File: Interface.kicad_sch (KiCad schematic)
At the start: 39 parts, among them U11 WE-TVS-82400102, U2 SN74LVC2G14DBV, U6 THVD1400D, U7 TLP2310, U8 TLP2310

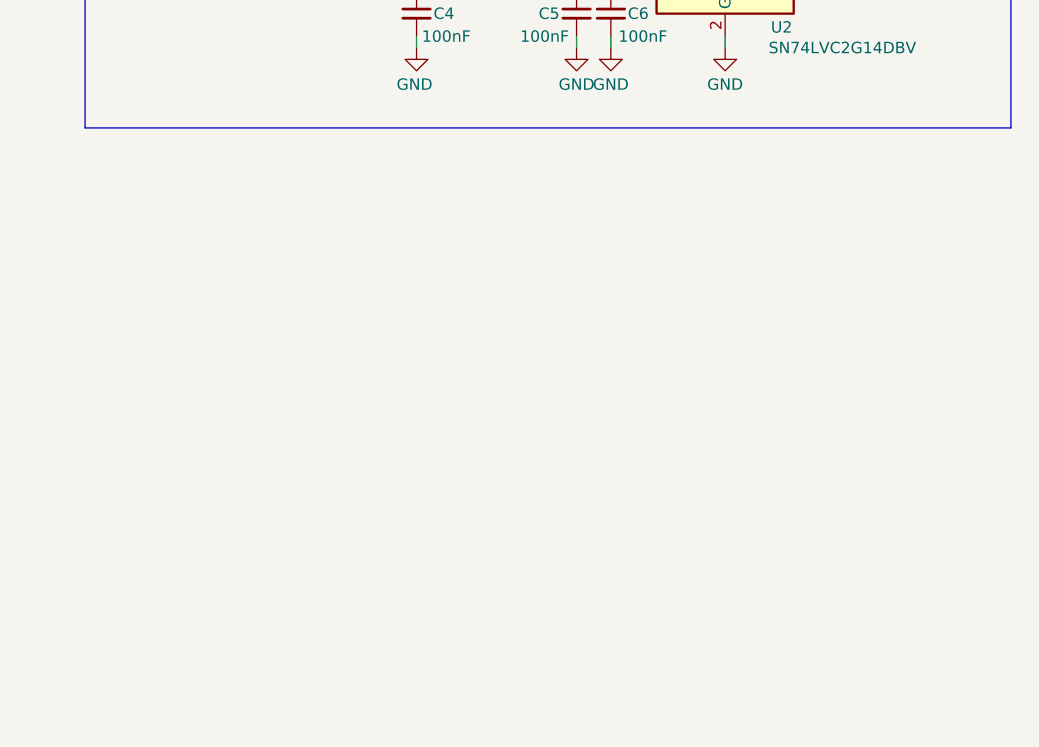
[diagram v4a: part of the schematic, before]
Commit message: feat(hw): add asymmetrical RC pulse stretcher for UART TX/RX activity LEDs
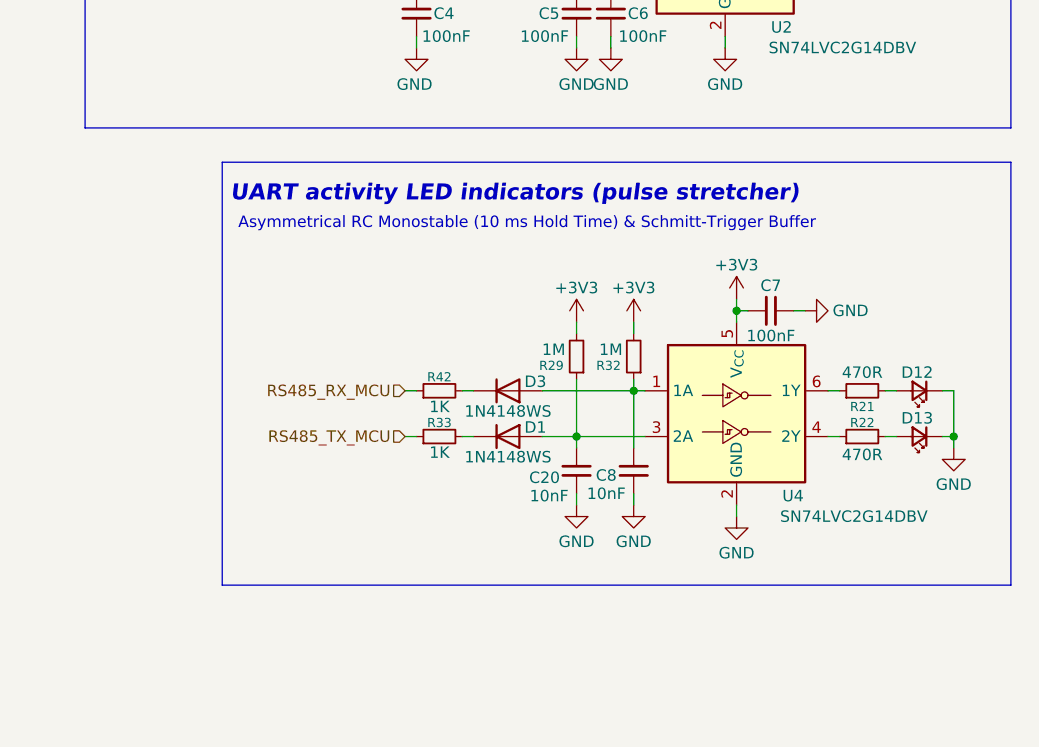
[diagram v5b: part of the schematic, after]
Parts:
- added C20, C8: 10nF, Capacitor_SMD:C_0603_1608Metric, symbol Device:C_Small
- added C7: 100nF, Capacitor_SMD:C_0603_1608Metric, symbol Device:C_Small
- added D1, D3: 1N4148WS, Diode_SMD:D_SOD-323, symbol Diode:1N4148WS
- added D12, D13: LED_Small, LED_SMD:LED_0603_1608Metric, symbol Device:LED_Small
- added R21, R22: 470R, Resistor_SMD:R_0603_1608Metric, symbol Device:R_Small
- added R29, R32: 1M, Resistor_SMD:R_0603_1608Metric, symbol Device:R_Small
- added R33, R42: 1K, Resistor_SMD:R_0603_1608Metric, symbol Device:R_Small
- added U4: SN74LVC2G14DBV, Package_TO_SOT_SMD:SOT-23-6, symbol 74xGxx:SN74LVC2G14DBV
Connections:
- net +3V3: now also C7.1, R29.2, R32.2, U4.5 (V_{CC})
- net GND: now also C20.1, C7.2, C8.1, D12.1 (K), D13.1 (K), U4.2 (GND)
- net RS485_RX_MCU: now also R42.1
- net RS485_TX_MCU: now also R33.1
- new net: C20.2, D1.2 (A), R29.1, U4.3 (2A)
- new net: R21.1, U4.6 (1Y)
- new net: D12.2 (A), R21.2
- new net: D1.1 (K), R33.2
- new net: C8.2, D3.2 (A), R32.1, U4.1 (1A)
- new net: R22.1, U4.4 (2Y)
- new net: D13.2 (A), R22.2
- new net: D3.1 (K), R42.2
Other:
- note added: "Asymmetrical RC Monostable (10 ms Hold Time) & Schmitt-Trigger Buffer"
- note added: "UART activity LED indicators (pulse stretcher)"

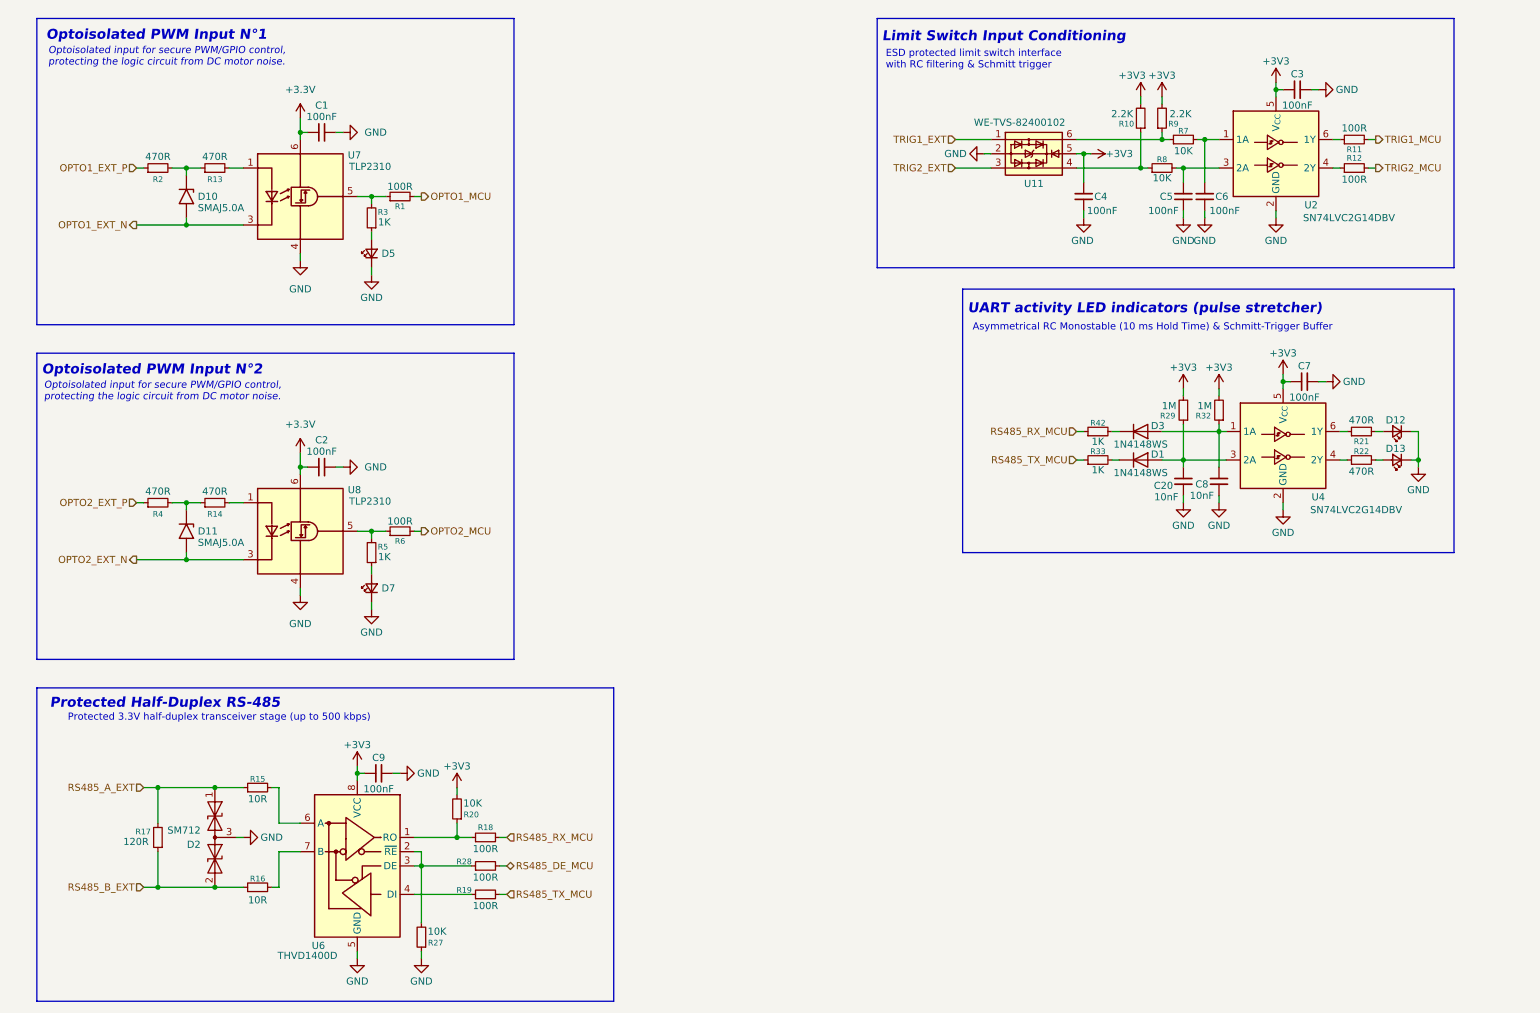
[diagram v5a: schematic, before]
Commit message: feat:add power sheat
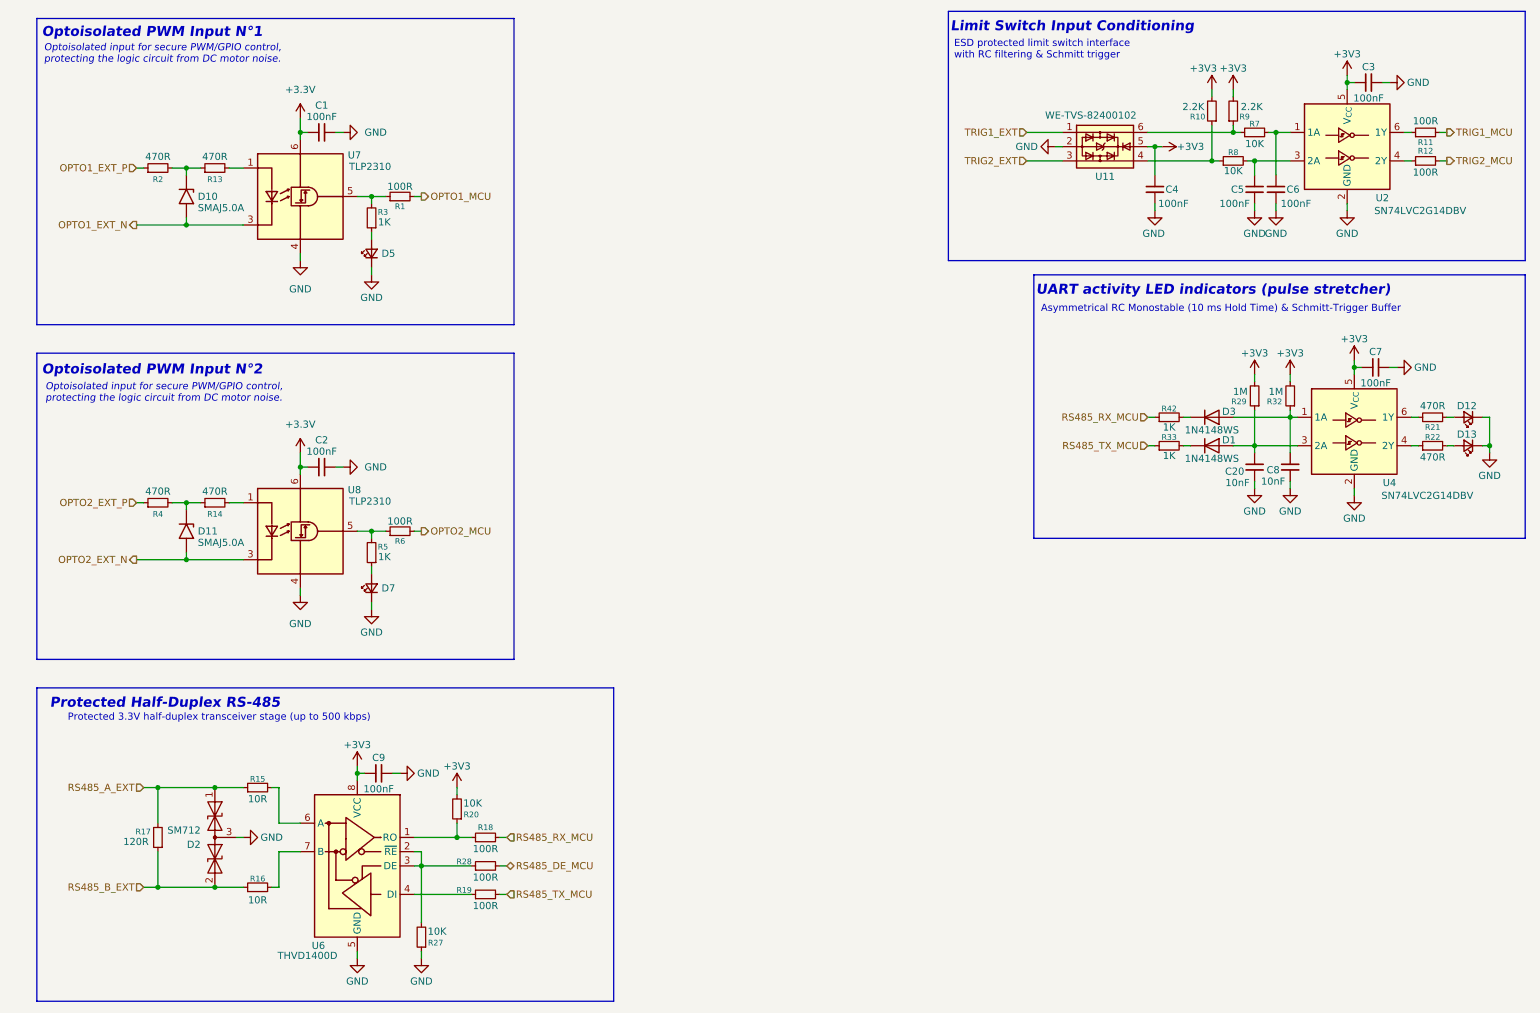
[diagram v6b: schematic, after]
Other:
- moved on the sheet: C20, C3, C4, C5, C6, C7, C8, D1, D12, D13, D3, R10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

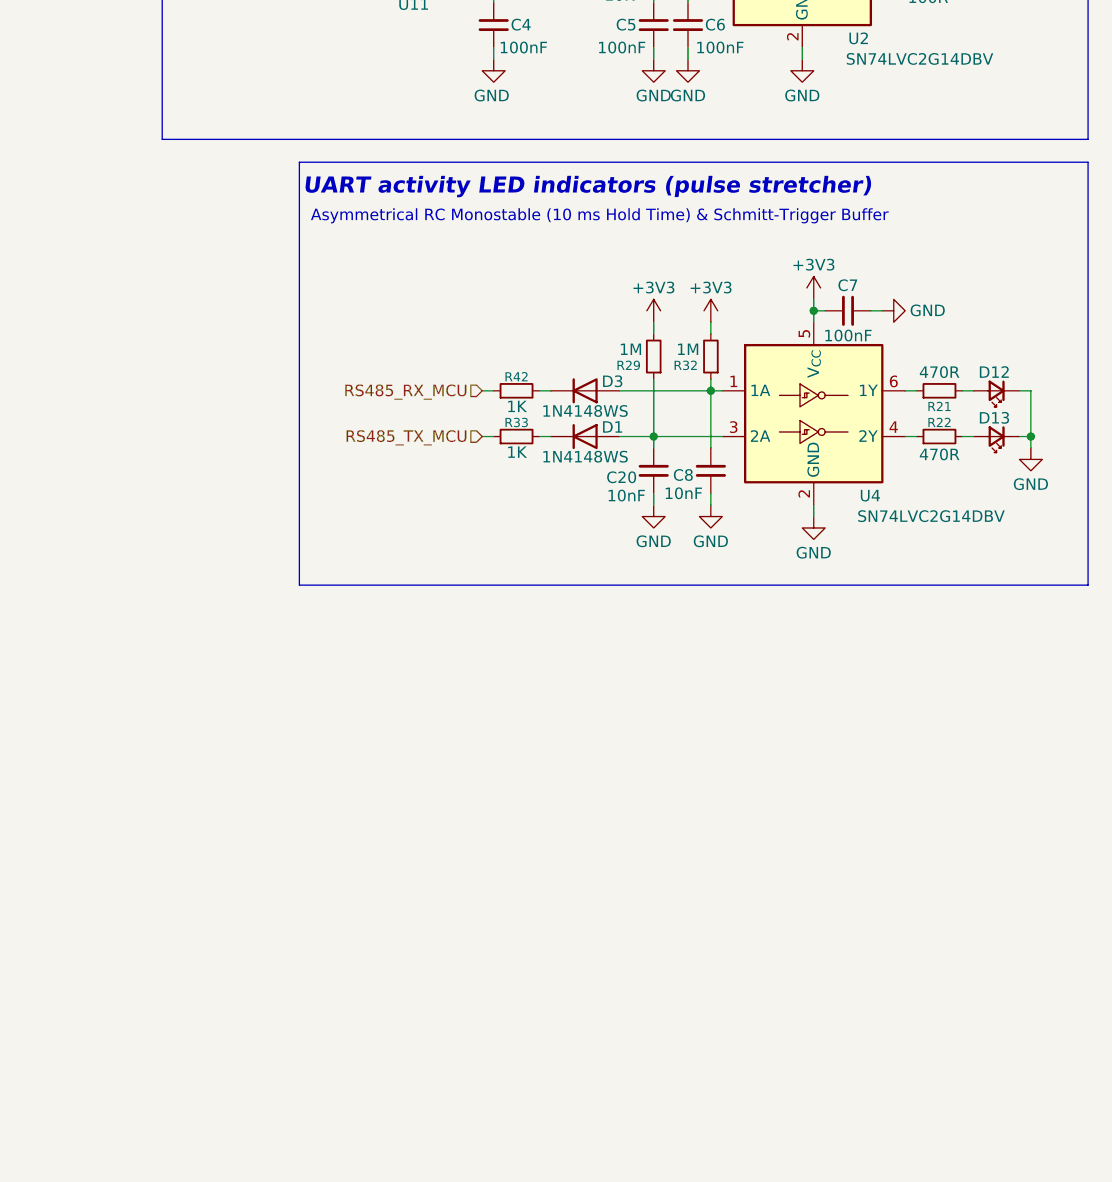
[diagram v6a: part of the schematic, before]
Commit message: feat: add quadrature encoder interface
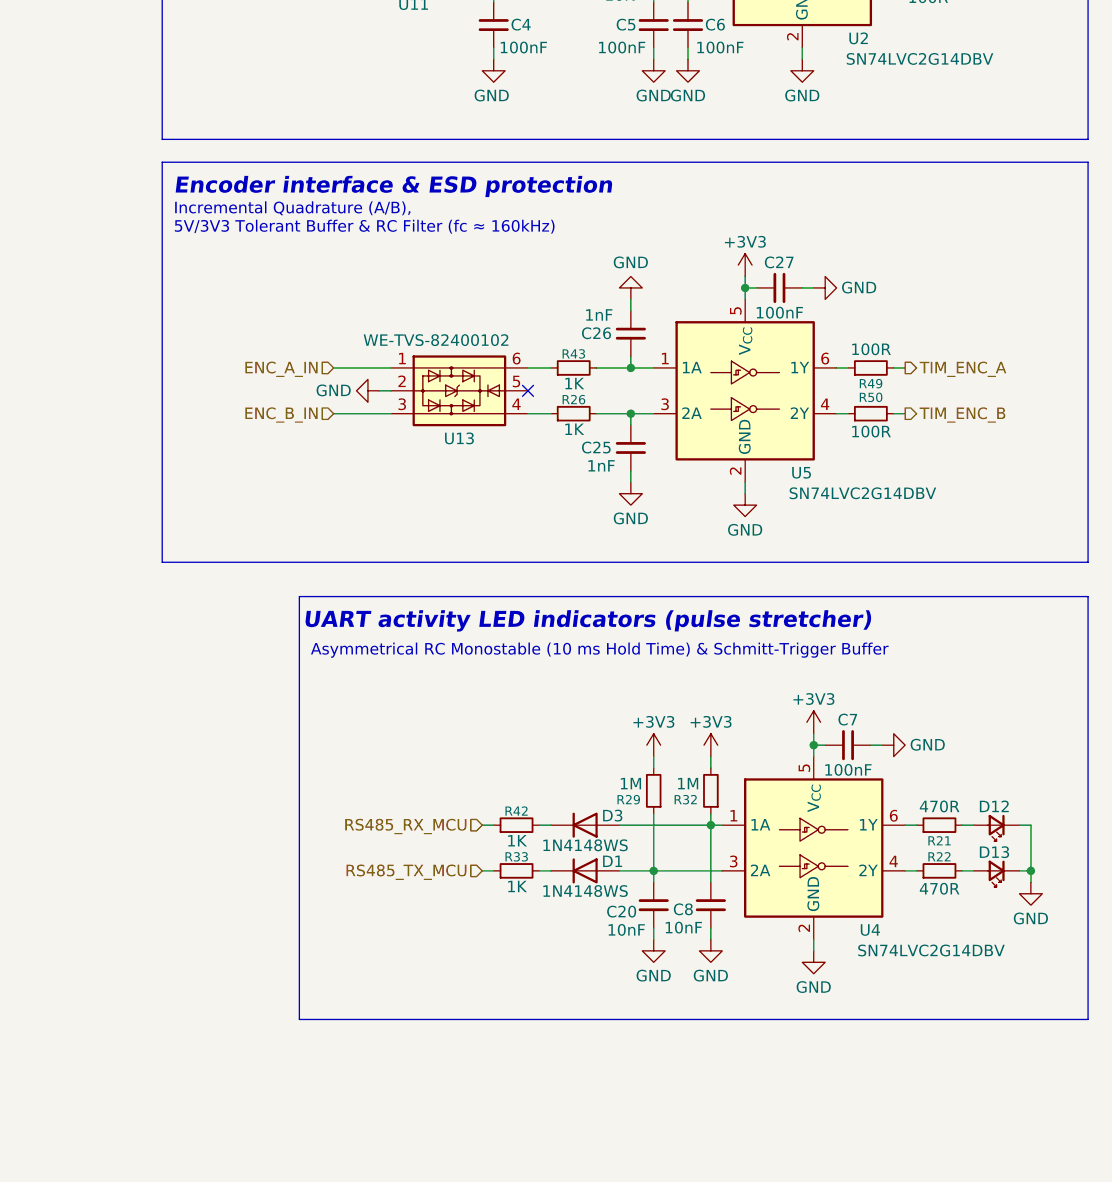
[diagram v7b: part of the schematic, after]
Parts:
- added C25, C26: 1nF, Capacitor_SMD:C_0603_1608Metric, symbol Device:C_Small
- added C27: 100nF, Capacitor_SMD:C_0603_1608Metric, symbol Device:C_Small
- added R26, R43: 1K, Resistor_SMD:R_0603_1608Metric, symbol Device:R_Small
- added R49, R50: 100R, Resistor_SMD:R_0603_1608Metric, symbol Device:R_Small
- added U13: WE-TVS-82400102, Package_TO_SOT_SMD:SOT-23-6, symbol Power_Protection:WE-TVS-82400102
- added U5: SN74LVC2G14DBV, Package_TO_SOT_SMD:SOT-23-6, symbol 74xGxx:SN74LVC2G14DBV
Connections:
- net +3V3: now also C27.1, U5.5 (V_{CC})
- net GND: now also C25.1, C26.1, C27.2, U13.2, U5.2 (GND)
- new net: R26.1, U13.4
- new net: C25.2, R26.2, U5.3 (2A)
- new net: R50.1, U5.4 (2Y)
- new net: C26.2, R43.2, U5.1 (1A)
- new net: R43.1, U13.6
- new net: R49.1, U5.6 (1Y)
- new net ENC_A_IN: U13.1
- new net ENC_B_IN: U13.3
- new net TIM_ENC_A: R49.2
- new net TIM_ENC_B: R50.2
- no-connect marks 0 -> 1
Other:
- note added: "Encoder interface & ESD protection"
- note added: "Incremental Quadrature (A/B), 5V/3V3 Tolerant Buffer & RC Filter (fc ≈ 160kHz)"
- moved on the sheet: C20, C7, C8, D1, D12, D13, D3, R21, R22, R29, R32, R33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

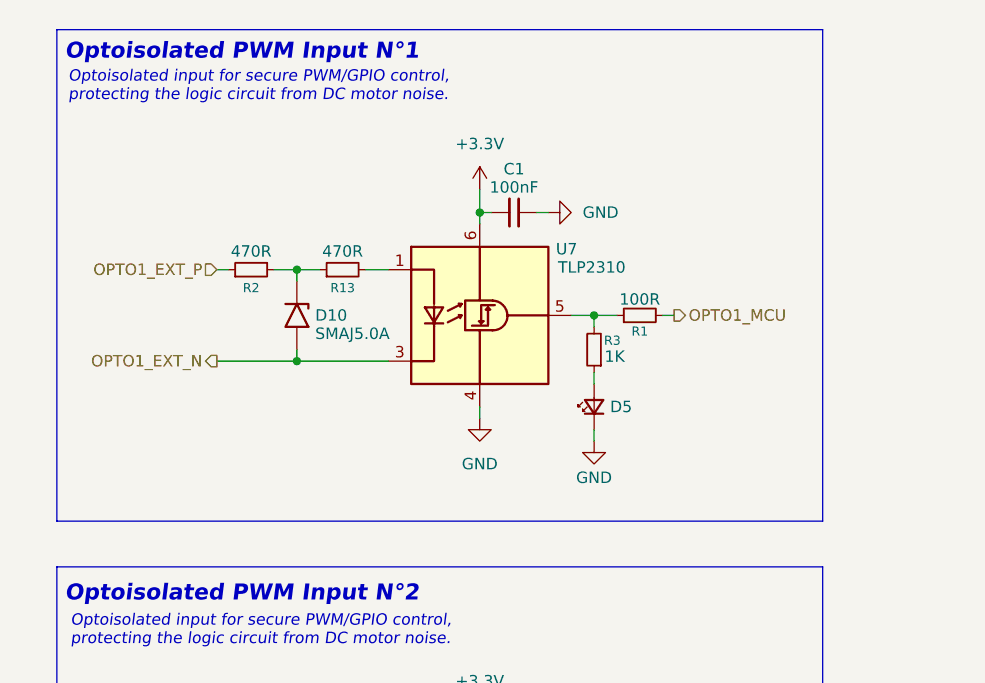
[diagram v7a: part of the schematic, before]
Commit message: feat: add LTC4365 protection circuit and 3.3V logic LDO
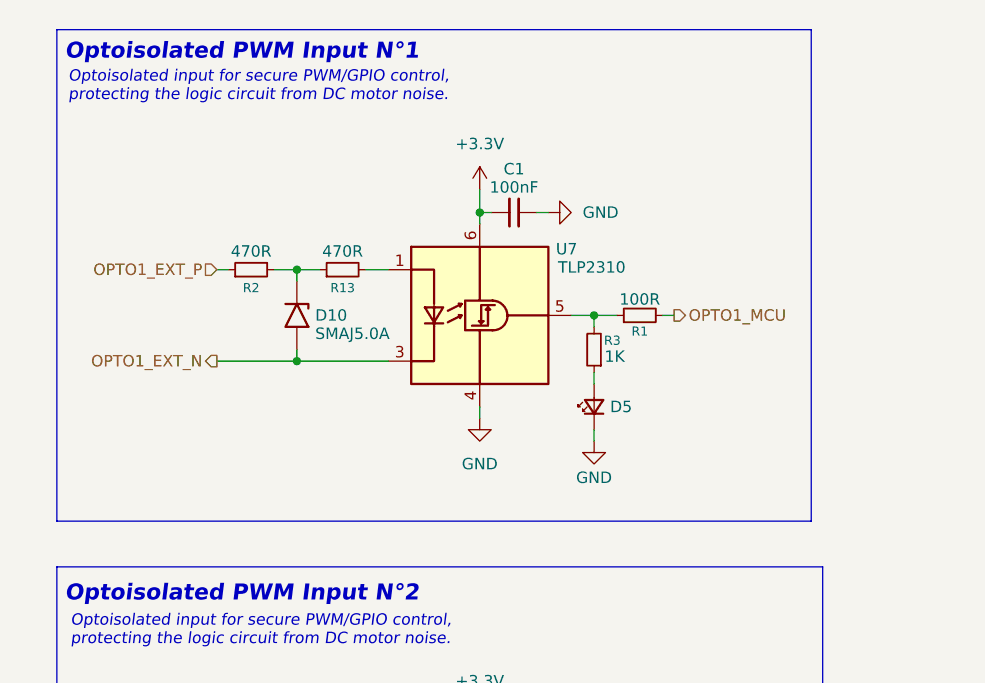
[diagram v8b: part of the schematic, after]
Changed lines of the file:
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@@
 	(rectangle
 		(start 16.51 16.51)
-		(end 101.6 71.12)
+		(end 100.33 71.12)
 		(stroke
 			(width 0.0508)
